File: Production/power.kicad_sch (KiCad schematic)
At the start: 5 parts, among them U204 TPS62177DQCR

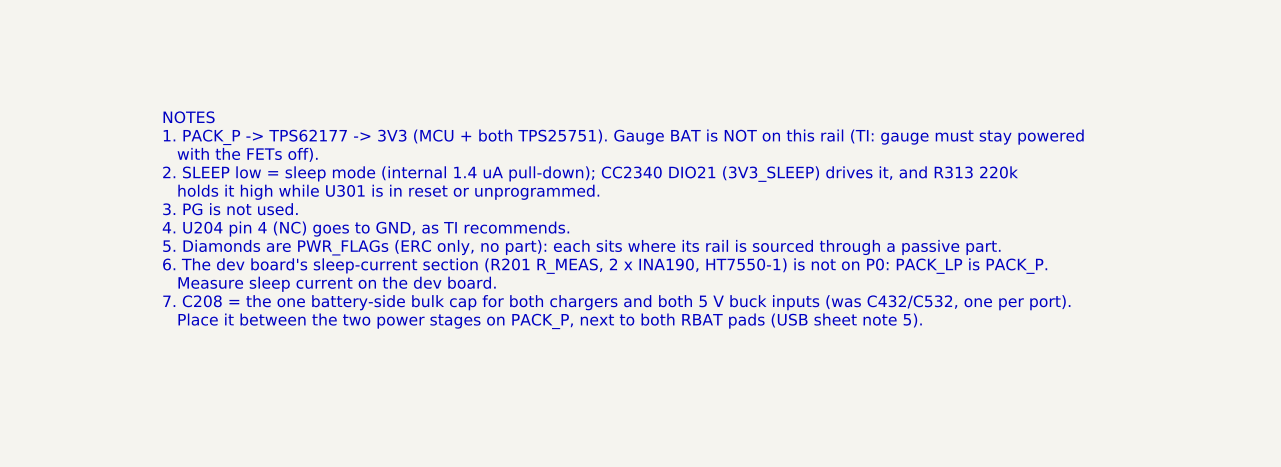
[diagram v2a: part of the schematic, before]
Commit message: Production P0 is the first build: gauge training access and tuning hedges
Dev board skipped. J302 = second TC2030-NL (GAUGE: SDA, CHG_INH, NRST, GND,
SCL) replacing the SMBus pogo pads; J113/J114 PACK_P/GND load pads for the
learning cycle; R118 4.7k + TP113 WAKE pad. Hedges: R444-R447 back as 0R
0402 gate links, DNP 0402 snubbers. Probe pads (1.0 mm) VBUS/PPHV/PP5V/REGN/
SW1/SW2/GND per port. docs/production/p0-bringup-and-training.md. Netlist
check passes; ERC known warnings only. Board/.kicad_pro (user WIP) not included.

Co-Authored-By: Claude Opus 5.5 <noreply@anthropic.com>
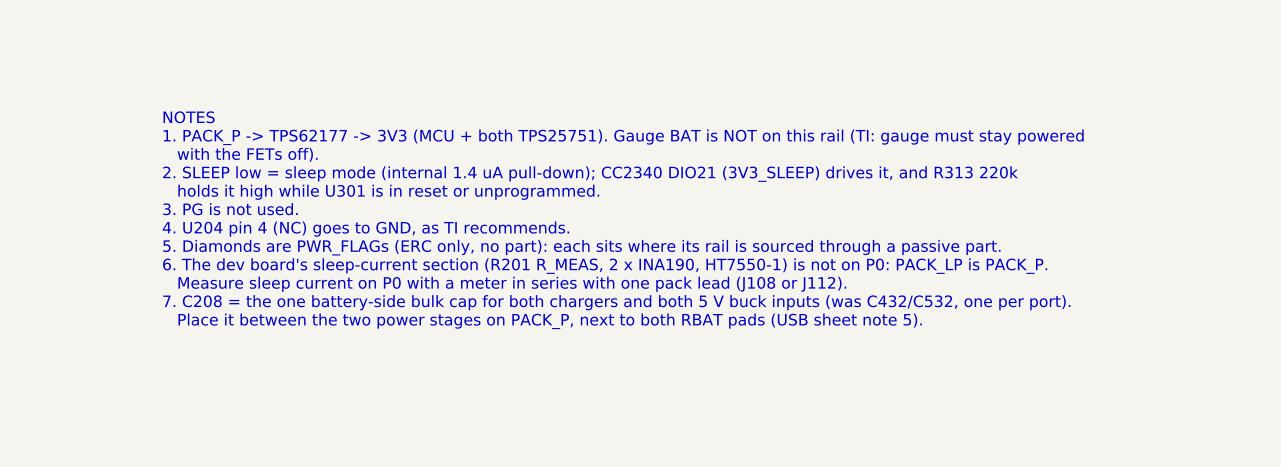
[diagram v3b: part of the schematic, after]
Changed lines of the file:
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@@
 		)
 	)
-	(text "NOTES\n1. PACK_P -> TPS62177 -> 3V3 (MCU + both TPS25751). Gauge BAT is NOT on this rail (TI: gauge must stay powered\n   with the FETs off).\n2. SLEEP low = sleep mode (internal 1.4 uA pull-down); CC2340 DIO21 (3V3_SLEEP) drives it, and R313 220k\n   holds it high while U301 is in reset or unprogrammed.\n3. PG is not used.\n4. U204 pin 4 (NC) goes to GND, as TI recommends.\n5. Diamonds are PWR_FLAGs (ERC only, no part): each sits where its rail is sourced through a passive part.\n6. The dev board's sleep-current section (R201 R_MEAS, 2 x INA190, HT7550-1) is not on P0: PACK_LP is PACK_P.\n   Measure sleep current on the dev board.\n7. C208 = the one battery-side bulk cap for both chargers and both 5 V buck inputs (was C432/C532, one per port).\n   Place it between the two power stages on PACK_P, next to both RBAT pads (USB sheet note 5)."
+	(text "NOTES\n1. PACK_P -> TPS62177 -> 3V3 (MCU + both TPS25751). Gauge BAT is NOT on this rail (TI: gauge must stay powered\n   with the FETs off).\n2. SLEEP low = sleep mode (internal 1.4 uA pull-down); CC2340 DIO21 (3V3_SLEEP) drives it, and R313 220k\n   holds it high while U301 is in reset or unprogrammed.\n3. PG is not used.\n4. U204 pin 4 (NC) goes to GND, as TI recommends.\n5. Diamonds are PWR_FLAGs (ERC only, no part): each sits where its rail is sourced through a passive part.\n6. The dev board's sleep-current section (R201 R_MEAS, 2 x INA190, HT7550-1) is not on P0: PACK_LP is PACK_P.\n   Measure sleep current on P0 with a meter in series with one pack lead (J108 or J112).\n7. C208 = the one battery-side bulk cap for both chargers and both 5 V buck inputs (was C432/C532, one per port).\n   Place it between the two power stages on PACK_P, next to both RBAT pads (USB sheet note 5)."
 		(exclude_from_sim no)
 		(at 215.9 129.54 0)
@@
 		(in_pos_files yes)
 		(dnp no)
-		(property "Reference" "#PWR9009"
+		(property "Reference" "#PWR9011"
 			(at 63.5 129.54 0)
 			(hide yes)
@@
 			(project "Monolith"
 				(path "/f83241ae-2bb3-4ed7-b986-c0a03971de0a/d9806540-c841-409c-9faa-82254b30b220"
-					(reference "#PWR9010")
+					(reference "#PWR9012")
 					(unit 1)
 				)
@@
 		(in_pos_files yes)
 		(dnp no)
-		(property "Reference" "#PWR9011"
+		(property "Reference" "#PWR9013"
 			(at 63.5 137.16 0)
 			(hide yes)
@@
 			(project "Monolith"
 				(path "/f83241ae-2bb3-4ed7-b986-c0a03971de0a/d9806540-c841-409c-9faa-82254b30b220"
-					(reference "#PWR9012")
+					(reference "#PWR9014")
 					(unit 1)
 				)
@@
 		(in_pos_files yes)
 		(dnp no)
-		(property "Reference" "#PWR9013"
+		(property "Reference" "#PWR9015"
 			(at 190.5 59.69 0)
 			(hide yes)
@@
 			(project "Monolith"
 				(path "/f83241ae-2bb3-4ed7-b986-c0a03971de0a/d9806540-c841-409c-9faa-82254b30b220"
-					(reference "#PWR9014")
+					(reference "#PWR9016")
 					(unit 1)
 				)
@@
 		(in_pos_files yes)
 		(dnp no)
-		(property "Reference" "#PWR9015"
+		(property "Reference" "#PWR9017"
 			(at 121.92 59.69 0)
 			(hide yes)
@@
 			(project "Monolith"
 				(path "/f83241ae-2bb3-4ed7-b986-c0a03971de0a/d9806540-c841-409c-9faa-82254b30b220"
-					(reference "#PWR9016")
+					(reference "#PWR9018")
 					(unit 1)
 				)

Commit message: Production schematic P0: layout clean-up pass
New tools/layout_production.py (after make and tidy): block moves via
DevBoard/tools/move_region.py, then place_fields.py and check_overlaps.py.
Gauge: pack/NTC pads compacted, current sense and test/training pads moved up;
MCU: blocks regrouped, notes moved, J302 at 5.08 mm pin pitch; 3V3 Rail:
shared bulk and notes beside the rail; stale headings and index text fixed.
0 overlaps on all sheets; netlist check passes; ERC known warnings only.

Co-Authored-By: Claude Opus 5.5 <noreply@anthropic.com>
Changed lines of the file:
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@@
 	(text "NOTES\n1. PACK_P -> TPS62177 -> 3V3 (MCU + both TPS25751). Gauge BAT is NOT on this rail (TI: gauge must stay powered\n   with the FETs off).\n2. SLEEP low = sleep mode (internal 1.4 uA pull-down); CC2340 DIO21 (3V3_SLEEP) drives it, and R313 220k\n   holds it high while U301 is in reset or unprogrammed.\n3. PG is not used.\n4. U204 pin 4 (NC) goes to GND, as TI recommends.\n5. Diamonds are PWR_FLAGs (ERC only, no part): each sits where its rail is sourced through a passive part.\n6. The dev board's sleep-current section (R201 R_MEAS, 2 x INA190, HT7550-1) is not on P0: PACK_LP is PACK_P.\n   Measure sleep current on P0 with a meter in series with one pack lead (J108 or J112).\n7. C208 = the one battery-side bulk cap for both chargers and both 5 V buck inputs (was C432/C532, one per port).\n   Place it between the two power stages on PACK_P, next to both RBAT pads (USB sheet note 5)."
 		(exclude_from_sim no)
-		(at 215.9 129.54 0)
+		(at 220.98 83.82 0)
 		(effects
 			(font
@@
 		)
 		(property "Value" "GND"
-			(at 152.4 83.06 0)
+			(at 156.28 80.01 0)
 			(show_name no)
 			(do_not_autoplace no)
@@
 		)
 		(property "Value" "GND"
-			(at 165.1 67.82 0)
+			(at 165.10 67.82 0)
 			(show_name no)
 			(do_not_autoplace no)
@@
 		)
 		(property "Value" "GND"
-			(at 190.5 71.63 0)
+			(at 190.50 71.63 0)
 			(show_name no)
 			(do_not_autoplace no)
@@
 		)
 		(property "Value" "3V3"
-			(at 210.38 54.61 0)
+			(at 207.01 51.56 0)
 			(show_name no)
 			(do_not_autoplace no)
@@
 		(dnp no)
 		(property "Reference" "U204"
-			(at 152.4 49.59 0)
+			(at 152.40 49.59 0)
 			(show_name no)
 			(do_not_autoplace no)
@@
 		)
 		(property "Value" "TPS62177DQCR"
-			(at 152.4 51.56 0)
+			(at 152.40 51.56 0)
 			(show_name no)
 			(do_not_autoplace no)
@@
 	(symbol
 		(lib_id "Device:C_Polarized")
-		(at 63.5 133.35 0)
+		(at 63.5 105.41 0)
 		(unit 1)
 		(body_style 1)
@@
 		(dnp no)
 		(property "Reference" "C208"
-			(at 69.85 132.08 0)
+			(at 71.41 104.28 0)
 			(show_name no)
 			(do_not_autoplace no)
@@
 		)
 		(property "Value" "100u 25V"
-			(at 69.85 134.62 0)
+			(at 71.41 106.24 0)
 			(show_name no)
 			(do_not_autoplace no)
@@
 		)
 		(property "Footprint" "Capacitor_SMD:CP_Elec_6.3x7.7"
-			(at 64.46 129.54 0)
+			(at 64.46 101.6 0)
 			(hide yes)
 			(show_name no)
@@
 		)
 		(property "Datasheet" ""
-			(at 63.5 133.35 0)
+			(at 63.5 105.41 0)
 			(hide yes)
 			(show_name no)
@@
 		)
 		(property "Description" "Polarized capacitor"
-			(at 63.5 133.35 0)
+			(at 63.5 105.41 0)
 			(hide yes)
 			(show_name no)
@@
 		)
 		(property "Notes" "Shared PACK_P bulk for both chargers' battery sides and both TPS62933 inputs (replaces the per-port C432/C532). Place it between the two power stages, on PACK_P beside the RBAT pads: Production/tools/pack_bus_sims.py option A2"
-			(at 63.5 133.35 0)
+			(at 63.5 105.41 0)
 			(hide yes)
 			(show_name no)
@@
 		)
 		(property "LCSC" "C264047"
-			(at 63.5 133.35 0)
+			(at 63.5 105.41 0)
 			(hide yes)
 			(show_name no)
@@
 		)
 		(property "MPN" "Panasonic EEH-ZA1E101XP (hybrid polymer)"
-			(at 63.5 133.35 0)
+			(at 63.5 105.41 0)
 			(hide yes)
 			(show_name no)
@@
 	(symbol
 		(lib_id "power:VCC")
-		(at 63.5 129.54 0)
+		(at 63.5 101.6 0)
 		(unit 1)
 		(body_style 1)
@@
 		(dnp no)
 		(property "Reference" "#PWR9011"
-			(at 63.5 129.54 0)
+			(at 63.5 101.6 0)
 			(hide yes)
 			(show_name no)
@@
 		)
 		(property "Value" "PACK_P"
-			(at 63.5 125.22 0)
+			(at 63.50 97.28 0)
 			(show_name no)
 			(do_not_autoplace no)
@@
 		)
 		(property "Footprint" ""
-			(at 63.5 129.54 0)
+			(at 63.5 101.6 0)
 			(hide yes)
 			(show_name no)
@@
 		)
 		(property "Datasheet" ""
-			(at 63.5 129.54 0)
+			(at 63.5 101.6 0)
 			(hide yes)
 			(show_name no)
@@
 		)
 		(property "Description" "Power symbol creates a global label with name \"VCC\""
-			(at 63.5 129.54 0)
+			(at 63.5 101.6 0)
 			(hide yes)
 			(show_name no)
@@
 	(symbol
 		(lib_id "power:GND")
-		(at 63.5 137.16 0)
+		(at 63.5 109.22 0)
 		(unit 1)
 		(body_style 1)
@@
 		(dnp no)
 		(property "Reference" "#PWR9013"
-			(at 63.5 137.16 0)
+			(at 63.5 109.22 0)
 			(hide yes)
 			(show_name no)
@@
 		)
 		(property "Value" "GND"
-			(at 63.5 141.48 0)
+			(at 63.50 113.54 0)
 			(show_name no)
 			(do_not_autoplace no)
@@
 		)
 		(property "Footprint" ""
-			(at 63.5 137.16 0)
+			(at 63.5 109.22 0)
 			(hide yes)
 			(show_name no)
@@
 		)
 		(property "Datasheet" ""
-			(at 63.5 137.16 0)
+			(at 63.5 109.22 0)
 			(hide yes)
 			(show_name no)
@@
 		)
 		(property "Description" "Power symbol creates a global label with name \"GND\" , ground"
-			(at 63.5 137.16 0)
+			(at 63.5 109.22 0)
 			(hide yes)
 			(show_name no)
@@
 	(text "PACK_P SHARED BULK  (both chargers + both 5 V buck inputs)"
 		(exclude_from_sim no)
-		(at 40.64 116.84 0)
+		(at 40.64 88.9 0)
 		(effects
 			(font
@@
 		)
 		(property "Value" "PACK_P"
-			(at 121.92 62.74 0)
-			(show_name no)
-			(do_not_autoplace no)
+			(at 121.92 54.10 0)
+			(show_name no)
+			(do_not_autoplace no)

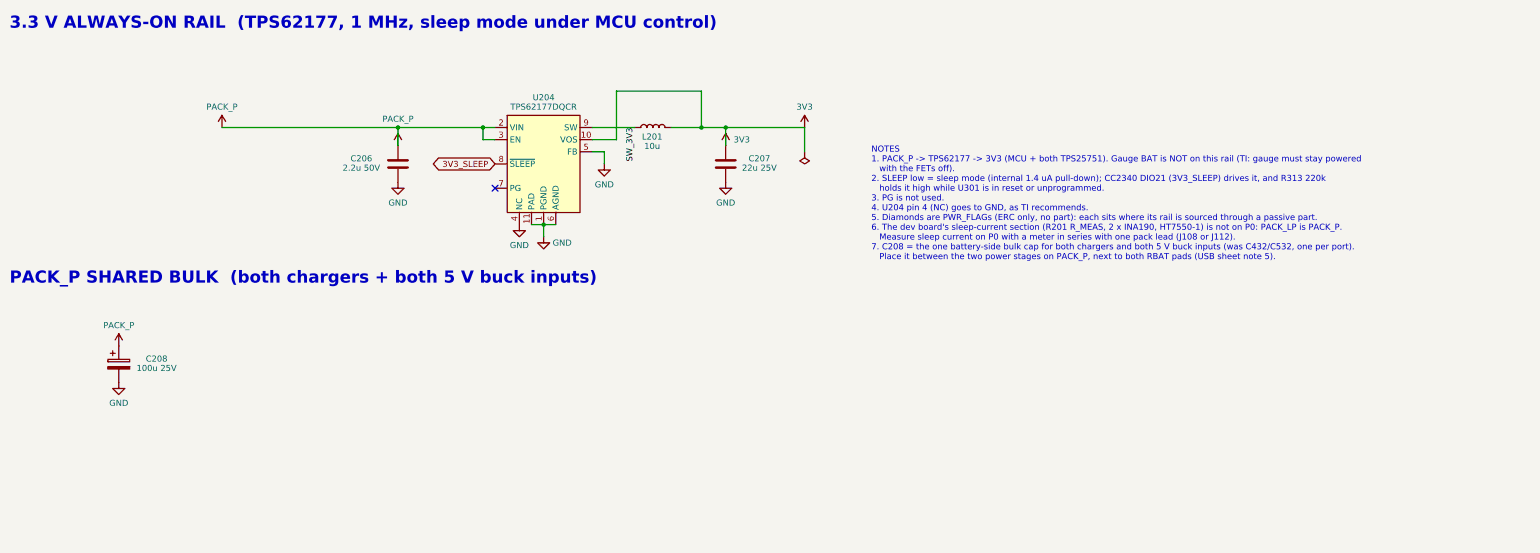
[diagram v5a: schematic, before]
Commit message: Production: low-profile bulk, nothing taller than the 3.1 mm inductors
USB side per port: C421 100u can -> KEMET T521D 33u 35V polymer tantalum,
plus C457 (second T521D) and C456 (fifth 22u 35V 1210): 83 uF worst at 20 V.
PACK_P: C208 hybrid -> C208-C213, six GMK325 22u 35V 1210; C431/C434/C444 ->
the same part: 86 uF worst at 16.8 V, all MLCC (polymer chips' leakage
rating is too high for the always-live bus). C427 leaves the cut list.
Checked with tools/low_profile_sims.py (options L2 / N1).

Co-Authored-By: Claude Opus 5.5 <noreply@anthropic.com>
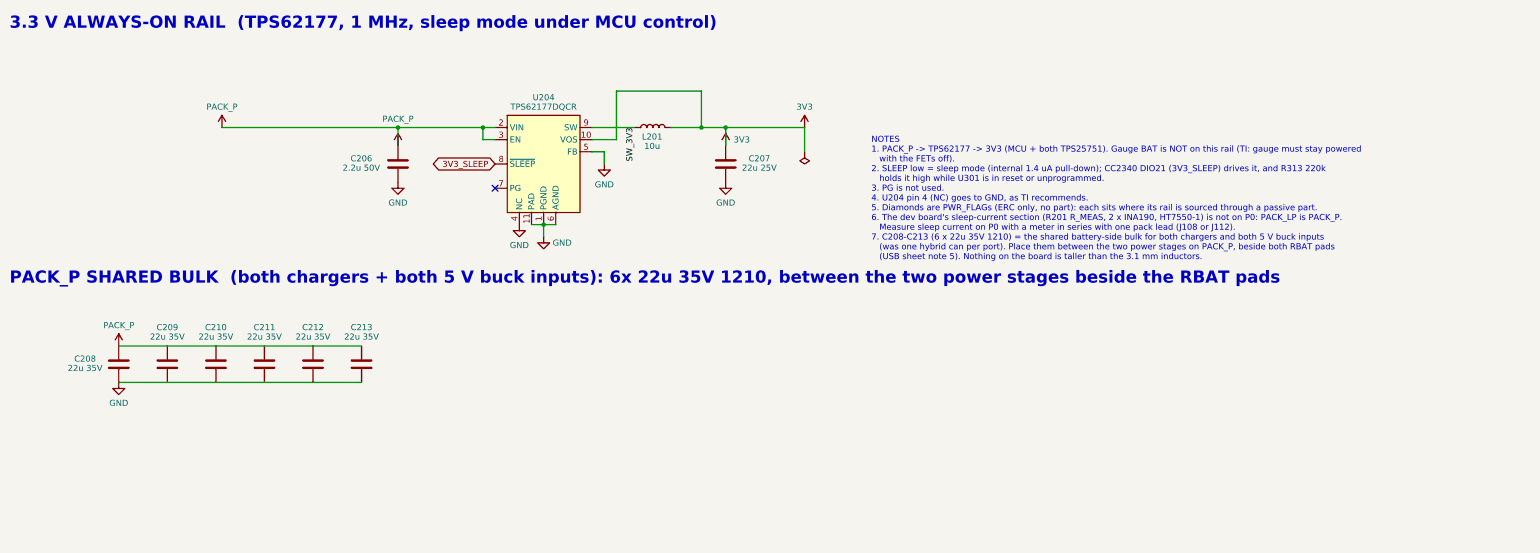
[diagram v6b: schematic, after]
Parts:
- removed C208: 100u 25V, Capacitor_SMD:CP_Elec_6.3x7.7, symbol Device:C_Polarized
- added C208, C209, C210, C211, C212, C213: 22u 35V, Capacitor_SMD:C_1210_3225Metric, symbol Device:C
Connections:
- net GND: now also C208.2, C209.2, C210.2, C211.2, C212.2, C213.2
- net PACK_P: now also C208.1, C209.1, C210.1, C211.1, C212.1, C213.1
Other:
- note added: "PACK_P SHARED BULK (both chargers + both 5 V buck inputs): 6x 22u 35V 1210, between the two power stages beside the RBAT pads"
- note removed: "PACK_P SHARED BULK (both chargers + both 5 V buck inputs)"
